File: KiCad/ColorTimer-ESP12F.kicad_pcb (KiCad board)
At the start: 2 copper layers, 72 x 47 mm, 40 parts, among them J1 SW_CON, J2 USB_B_Micro, J3 COLOER_LED, J4 AkitsukiCON, J5 GPIO_CON, J6 POWER_CON, Q1 2N7000, Q2 2N7000, SW1 RESET, SW2 Trigger SW, SW3 FLASH, SW4 SW_SPDT, U1 ESP-12F, U2 CH340K, U3 BA033CC0T_TO220

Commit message: 表面実装部品版 作成開始
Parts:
- removed C3: 10u, Capacitor_THT:C_Disc_D3.0mm_W1.6mm_P2.50mm
- removed C4: 1u, Capacitor_THT:C_Disc_D3.0mm_W1.6mm_P2.50mm
- removed C7: 22u, Capacitor_THT:CP_Radial_D5.0mm_P2.50mm
- removed Q1, Q2: 2N7000, Package_TO_SOT_THT:TO-92_Inline_Wide
- removed R6: 33, Resistor_THT:R_Axial_DIN0207_L6.3mm_D2.5mm_P10.16mm_Horizontal
- removed SW3: FLASH, Button_Switch_THT:SW_PUSH_6mm_H8mm
- removed U3: BA033CC0T_TO220, Package_TO_SOT_THT:TO-220-3_Vertical
- added D4: D_Schottky, Diode_SMD:D_SOD-123, F.Cu at (106.6, 64.3)
- added J7: POWER_CON, Connector_JST:JST_XH_B2B-XH-A_1x02_P2.50mm_Vertical, F.Cu at (100.4, 53.1)
- C1, C2: footprint Capacitor_THT:C_Disc_D3.0mm_W1.6mm_P2.50mm -> Capacitor_SMD:C_0603_1608Metric_Pad1.08x0.95mm_HandSolder
- C5, C6: value 0.1u -> 22u; footprint Capacitor_THT:C_Disc_D3.0mm_W1.6mm_P2.50mm -> Capacitor_SMD:C_0603_1608Metric_Pad1.08x0.95mm_HandSolder
- D1, D2, D3: footprint LED_THT:LED_D3.0mm -> LED_SMD:LED_0603_1608Metric_Pad1.05x0.95mm_HandSolder
- J1: footprint Connector_PinSocket_2.54mm:PinSocket_1x02_P2.54mm_Vertical -> Connector_JST:JST_XH_B2B-XH-A_1x02_P2.50mm_Vertical
- J2: value USB_B_Micro -> OLED; footprint Connector_USB:USB_Micro-B_Molex-105017-0001 -> Connector_JST:JST_XH_B4B-XH-A_1x04_P2.50mm_Vertical
- J3: footprint Connector_PinSocket_2.54mm:PinSocket_1x03_P2.54mm_Vertical -> Connector_JST:JST_XH_B3B-XH-A_1x03_P2.50mm_Vertical
- J4: value AkitsukiCON -> Ext_Con; footprint AE:AE-USB-MICRO-B-D -> Connector_JST:JST_XH_B3B-XH-A_1x03_P2.50mm_Vertical
- J5: value GPIO_CON -> Downloader_CON; footprint Connector_PinSocket_2.54mm:PinSocket_1x09_P2.54mm_Vertical -> Connector_PinSocket_2.54mm:PinSocket_1x06_P2.54mm_Vertical
- J6: value POWER_CON -> POWER_SW_CON; footprint Connector_PinSocket_2.54mm:PinSocket_1x02_P2.54mm_Vertical -> Connector_JST:JST_XH_B2B-XH-A_1x02_P2.50mm_Vertical
- R1, R10, R2, R3, R7, R8, R9: footprint Resistor_THT:R_Axial_DIN0207_L6.3mm_D2.5mm_P10.16mm_Horizontal -> Resistor_SMD:R_0603_1608Metric_Pad0.98x0.95mm_HandSolder
- R4, R5: value 330 -> 1k; footprint Resistor_THT:R_Axial_DIN0207_L6.3mm_D2.5mm_P10.16mm_Horizontal -> Resistor_SMD:R_0603_1608Metric_Pad0.98x0.95mm_HandSolder
- SW1, SW2: footprint Button_Switch_THT:SW_PUSH_6mm_H8mm -> Button_Switch_SMD:SW_Push_SPST_NO_Alps_SKRK
- U2: value CH340K -> AMS1117-3.3; footprint Package_SO:SSOP-10-1EP_3.9x4.9mm_P1mm_EP2.1x3.3mm -> Package_TO_SOT_SMD:SOT-223-3_TabPin2
- moved H3 77.7 mm to (98.0, 83.9)
- moved J6 65.2 mm to (100.3, 62.2), turned to -90 degrees
- moved D3 62.7 mm to (102.8, 75.0), turned to 0 degrees
- moved SW4 61.6 mm to (102.8, 70.5)
- moved R10 59.8 mm to (98.7, 75.0)
- moved H2 58.0 mm to (139.0, 43.0)
- moved F1 51.7 mm to (110.1, 50.7), turned to -90 degrees
- moved SW2 45.1 mm to (116.7, 83.4), turned to 0 degrees
- moved U2 40.7 mm to (108.3, 58.3), turned to 90 degrees
- moved J4 39.9 mm to (124.0, 72.3)
- moved C6 38.4 mm to (106.0, 66.6), turned to 0 degrees
- moved C1 37.0 mm to (106.0, 46.2)
- moved J5 36.6 mm to (139.0, 50.5), turned to 0 degrees
- moved C5 35.0 mm to (109.8, 66.7), turned to 180 degrees
- moved J2 31.0 mm to (137.0, 76.5)
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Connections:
- C6 pad 1: EN -> +3.3V
- F1 pad 1: Net-(J2-VBUS) -> Net-(J7-Pin_1)
- J1 pad 1: /GPIO16 -> Net-(J1-Pin_1)
- J2 pad 1: Net-(J2-VBUS) -> /GPIO4
- J2 pad 2: Net-(J2-D-) -> /GPIO5
- J2 pad 3: Net-(J2-D+) -> +3.3V
- J2 pad 4: unconnected-(J2-ID-Pad4) -> GND
- J3 pad 1: /GPIO13 -> Net-(J3-Pin_1)
- J3 pad 2: Net-(J3-Pin_2) -> GND
- J3 pad 3: /GPIO12 -> Net-(J3-Pin_3)
- J4 pad 1: VCC -> /GPIO14
- J4 pad 2: Net-(J2-D-) -> /ADC
- J4 pad 3: Net-(J2-D+) -> GND
- J5 pad 1: /GPIO4 -> +3.3V
- J5 pad 2: /GPIO5 -> TxD
- J5 pad 3: /GPIO12 -> RxD
- J5 pad 4: /GPIO13 -> EN
- J5 pad 5: /GPIO14 -> GPIO0
- J5 pad 6: /GPIO16 -> GND
- R10 pad 2: VCC -> +5V
- R2 pad 2: /GPIO16 -> Net-(J1-Pin_1)
- R4 pad 2: /GPIO13 -> Net-(J3-Pin_1)
- R5 pad 2: /GPIO12 -> Net-(J3-Pin_3)
- SW2 pad 2: /GPIO16 -> Net-(J1-Pin_1)
- U1 pad 4: /GPIO16 -> Net-(J1-Pin_1)
- U1 pad 6: /GPIO12 -> Net-(J3-Pin_3)
- U1 pad 7: /GPIO13 -> Net-(J3-Pin_1)
- U2 pad 1: Net-(J2-D+) -> GND
- U2 pad 2: Net-(J2-D-) -> Net-(D4-A)
- U2 pad 3: GND -> +5V
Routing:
- net GND: track 205.0 -> 0.00 mm, vias 4 -> 0
- net +3.3V: track 106.1 -> 0.00 mm
- net /GPIO16: track 103.3 -> 0.00 mm
- net /GPIO12: track 79.5 -> 0.00 mm
- net /ADC: track 67.3 -> 0.00 mm
- net /GPIO13: track 64.6 -> 0.00 mm
- net /GPIO4: track 57.3 -> 0.00 mm
- net Net-(U1-REST): track 56.4 -> 0.00 mm
- net /GPIO5: track 55.0 -> 0.00 mm, vias 1 -> 0
- net GPIO0: track 53.5 -> 0.00 mm
- net /GPIO14: track 49.3 -> 0.00 mm
- net EN: track 44.9 -> 0.00 mm
- net VCC: track 43.0 -> 0.00 mm
- net TxD: track 36.0 -> 0.00 mm
- net RxD: track 31.0 -> 0.00 mm
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- removed copper zone on B.Cu, net GND
- removed copper zone on F.Cu, net GND
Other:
- board size 72 x 47 mm -> 47 x 47 mm
- board text added: "+3.3v"
- board text added: "3.3v >"
- board text added: "5V"
- board text added: "BLUE"
- board text added: "COLOR LED"
- board text added: "EN"
- board text added: "Ext Con"
- board text added: "GND >"
- board text added: "GPIO0"
- board text added: "PW SW"
- board text added: "RED"
- board text added: "RxD->TxD"
- board text added: "Trigger"
- board text added: "Trigger SW"
- board text added: "TxD->RxD"
- board text removed: "+3.3V"
- board text removed: "0.1u"
- board text removed: "10k"
- board text removed: "1k"
- board text removed: "1u"
- board text removed: "22u"
- board text removed: "33"
- board text removed: "330"
- board text removed: "ADC"
- board text removed: "BLUE LED"
- board text removed: "COLOR TIMER REV1 KUNI-NET 2025"
- board text removed: "FLASH"
- board text removed: "IO12"
- board text removed: "IO13"
- board text removed: "IO14"
- board text removed: "IO16"
- board text removed: "IO4"
- board text removed: "IO5"
- board text removed: "LED CON"
- board text removed: "MICRO-B"
- board text removed: "OFF ON"
- board text removed: "RED LED"
- board text removed: "SW CON"
- board text removed: "TRIGGER SW"

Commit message: REV2 表面実装部品版 ガーバーデータ出力
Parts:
- added J8: IO14_CON, Connector_JST:JST_XH_B2B-XH-A_1x02_P2.50mm_Vertical, F.Cu at (127.4, 72.6)
- added R11: 2.4k, Resistor_SMD:R_0603_1608Metric_Pad0.98x0.95mm_HandSolder, F.Cu at (134.8, 55.1)
- added R12: 2.4k, Resistor_SMD:R_0603_1608Metric_Pad0.98x0.95mm_HandSolder, F.Cu at (134.8, 52.2)
- J4: value Ext_Con -> ADC_CON; footprint Connector_JST:JST_XH_B3B-XH-A_1x03_P2.50mm_Vertical -> Connector_JST:JST_XH_B2B-XH-A_1x02_P2.50mm_Vertical
- moved J2 7.01 mm to (137.4, 69.5), turned to -90 degrees
- moved J4 5.59 mm to (118.4, 72.6)
- moved J1 4.89 mm to (109.3, 72.6)
- moved SW1 4.57 mm to (110.5, 50.7)
- moved F1 4.09 mm to (106.0, 50.6)
- moved D4 3.94 mm to (109.1, 67.4), turned to 180 degrees
- moved R7 2.56 mm to (134.8, 58.0), turned to 180 degrees
- moved R9 1.79 mm to (134.8, 61.0), turned to 180 degrees
- moved C5 1.77 mm to (110.1, 65.0)
- moved C6 1.63 mm to (106.2, 65.0), turned to 180 degrees
- moved R8 0.83 mm to (134.8, 63.7), turned to 0 degrees
- moved J6 0.67 mm to (100.8, 62.6)
- moved J7 0.56 mm to (100.8, 53.5)
- moved D1 0.13 mm to (109.9, 80.0), turned to 180 degrees
- moved U1 0.12 mm to (116.2, 49.9)
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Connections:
- C6 pad 1: +3.3V -> Net-(D4-A)
- J4 pad 1: /GPIO14 -> /ADC
- J4 pad 2: /ADC -> GND
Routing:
- net GND: track 0.00 -> 169.8 mm, vias 0 -> 7
- net +3.3V: track 0.00 -> 103.3 mm
- net Net-(J3-Pin_3): track 0.00 -> 54.0 mm
- net EN: track 0.00 -> 46.8 mm
- net Net-(J3-Pin_1): track 0.00 -> 41.2 mm
- net Net-(J1-Pin_1): track 0.00 -> 37.1 mm, vias 0 -> 2
- net +5V: track 0.00 -> 31.6 mm
- net /GPIO5: track 0.00 -> 25.6 mm, vias 0 -> 1
- net /GPIO4: track 0.00 -> 24.5 mm
- net /ADC: track 0.00 -> 22.1 mm, vias 0 -> 1
- net RxD: track 0.00 -> 22.0 mm
- net VCC: track 0.00 -> 21.3 mm
- net /GPIO14: track 0.00 -> 20.1 mm
- net Net-(U1-REST): track 0.00 -> 18.3 mm
- net TxD: track 0.00 -> 14.7 mm
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- added copper zone on B.Cu, net GND
- added copper zone on F.Cu, net GND
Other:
- board text added: "ADC GND"
- board text added: "Color Timer REV2 KUNI-NET 2025"
- board text added: "ESP32 Downloader"
- board text added: "GND 3.3v IO5 IO4"
- board text added: "IO14 GND"
- board text removed: "Ext Con"
- board text removed: "Trigger SW"

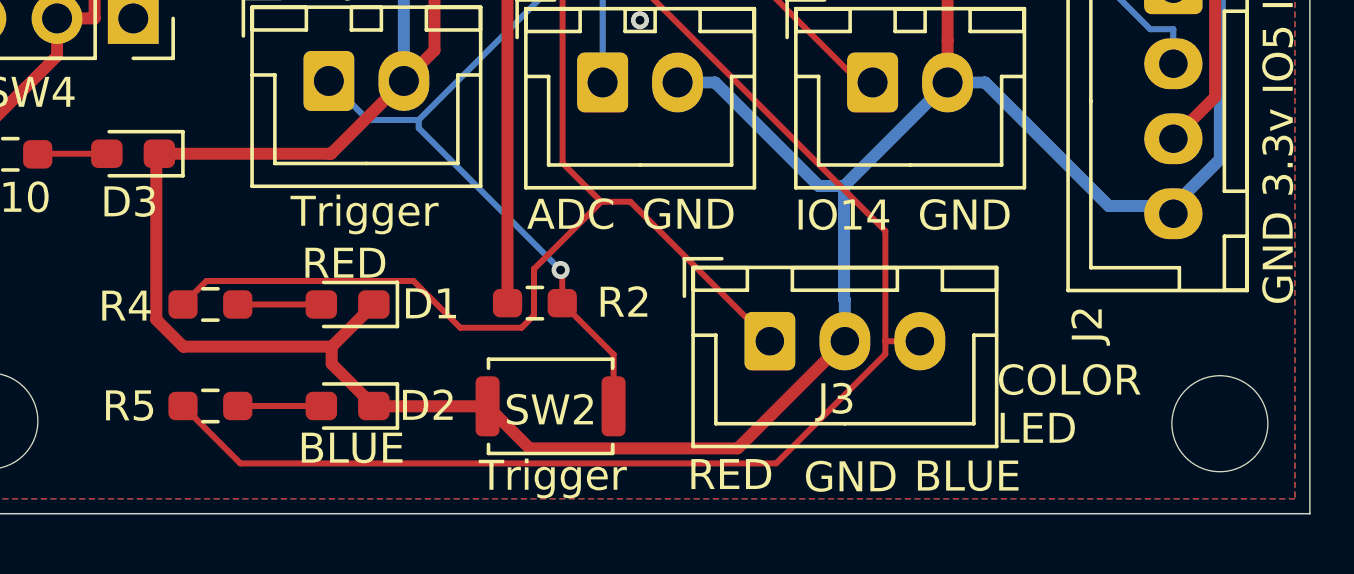
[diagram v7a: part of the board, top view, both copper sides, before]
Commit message: REV2 2色LEDのGNDに33Ω追加、ガーバー再出力 試作用
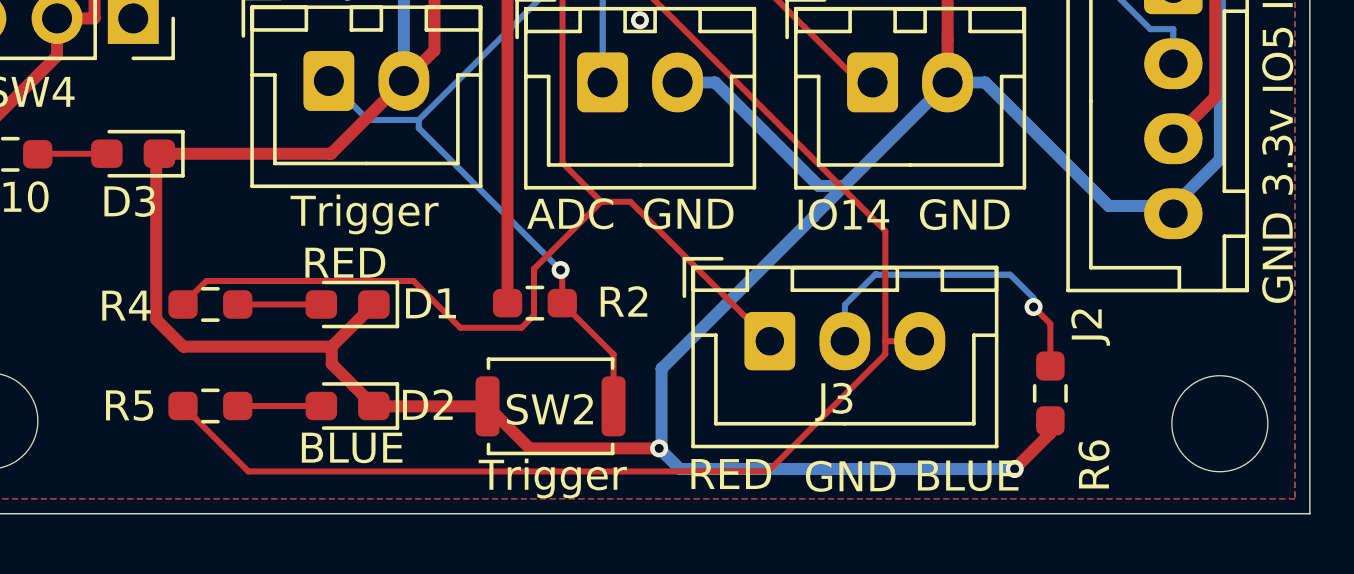
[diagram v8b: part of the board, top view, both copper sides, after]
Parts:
- added R6: 33, Resistor_SMD:R_0603_1608Metric_Pad0.98x0.95mm_HandSolder, F.Cu at (133.3, 83.0)
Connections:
- J3 pad 2: GND -> Net-(J3-Pin_2)
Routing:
- net GND: track 169.8 -> 182.5 mm, vias 7 -> 9
- net Net-(J3-Pin_2): track 0.00 -> 10.8 mm, vias 0 -> 1
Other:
- board text removed: "COLOR LED"
